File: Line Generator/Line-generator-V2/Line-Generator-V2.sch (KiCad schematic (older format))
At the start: 19 parts, among them J1 Conn_01x04

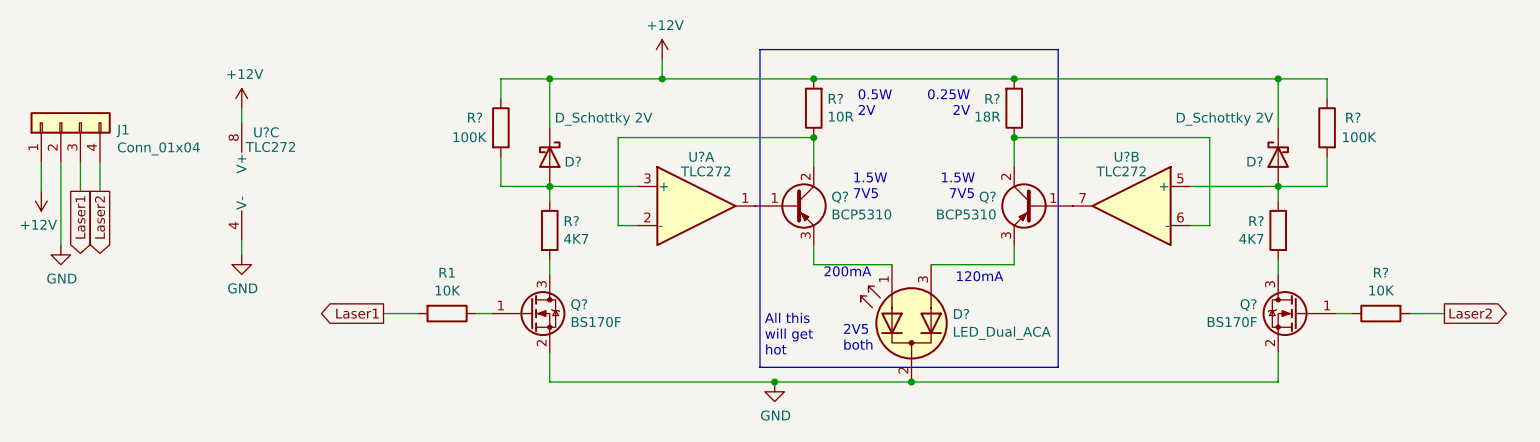
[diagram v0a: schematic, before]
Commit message: Now with 5V power...
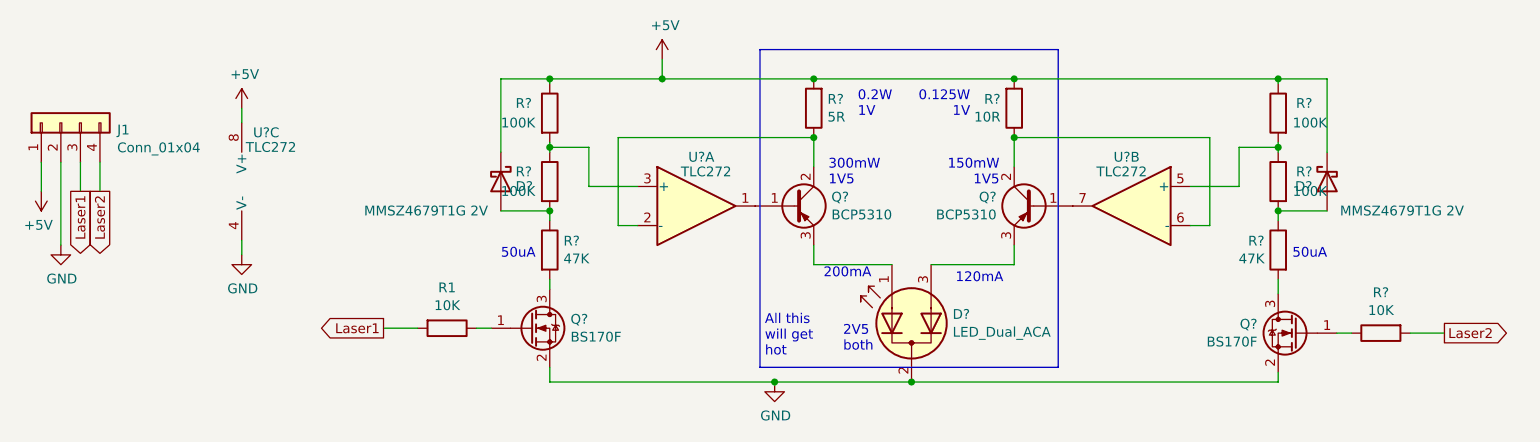
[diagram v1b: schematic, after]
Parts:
- removed D?: D_Schottky 2V, Diode_SMD:D_SOD-323_HandSoldering, symbol Device:D_Schottky
- removed R?: 100K, Resistor_SMD:R_0805_2012Metric_Pad1.15x1.40mm_HandSolder, symbol Device:R
- removed R?: 4K7, Resistor_SMD:R_0805_2012Metric_Pad1.15x1.40mm_HandSolder, symbol Device:R
- added D?: MMSZ4679T1G 2V, Diode_SMD:D_SOD-123, symbol Device:D_Schottky
- added R? (x3): 100K, Resistor_SMD:R_0805_2012Metric_Pad1.15x1.40mm_HandSolder, symbol Device:R
- added R?: 47K, Resistor_SMD:R_0805_2012Metric_Pad1.15x1.40mm_HandSolder, symbol Device:R
- D?: value D_Schottky 2V -> MMSZ4679T1G 2V; footprint Diode_SMD:D_SOD-323_HandSoldering -> Diode_SMD:D_SOD-123
- R?: value 10R -> 5R
- R?: value 4K7 -> 47K
- R?: value 18R -> 10R
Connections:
- net at D?.2 (A), R?.1: now also R?.2; no longer R?.2, U?.3 (+)
- net at U?.5 (+): now also R?.1, R?.2
- net at Q?.3 (D): now also R?.2
- net +12V renamed +5V
- net +5V: now also D?.1 (K), R?.1
- new net: R?.1, R?.2, U?.3 (+)
- new net: D?.2 (A), R?.1, R?.2
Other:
- note added: "0.125W\n1V"
- note added: "0.2W\n1V"
- note added: "150mW\n1V5"
- note added: "300mW\n1V5"
- note added: "50uA"
- note removed: "0.25W\n2V"
- note removed: "0.5W\n2V"
- note removed: "1.5W\n7V5"
- moved on the sheet: D?, Q?, R1, R?

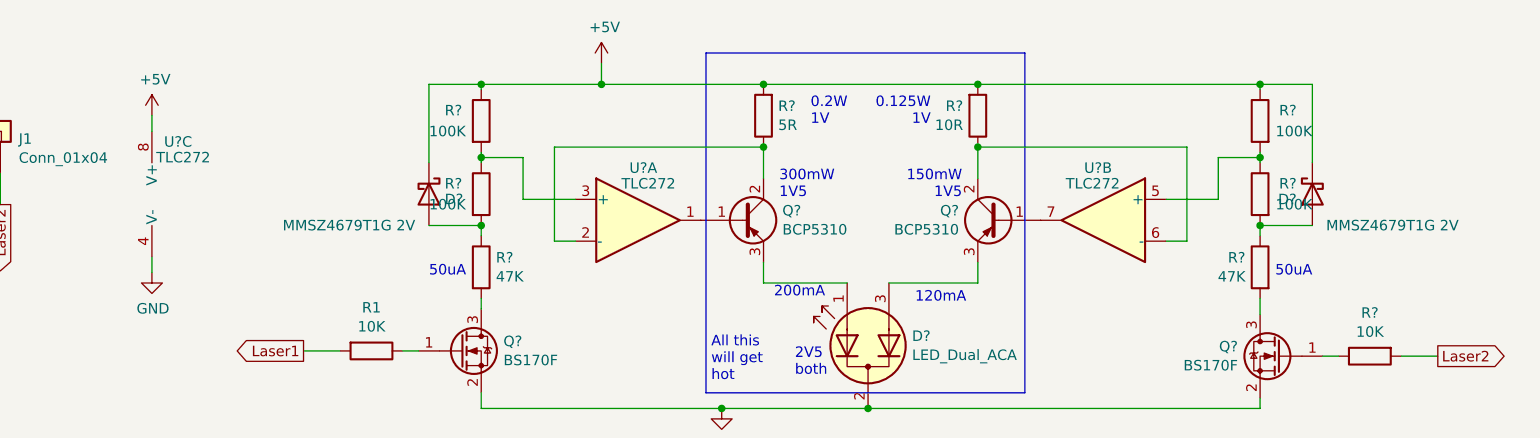
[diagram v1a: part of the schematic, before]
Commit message: Now with adjustable LED current.
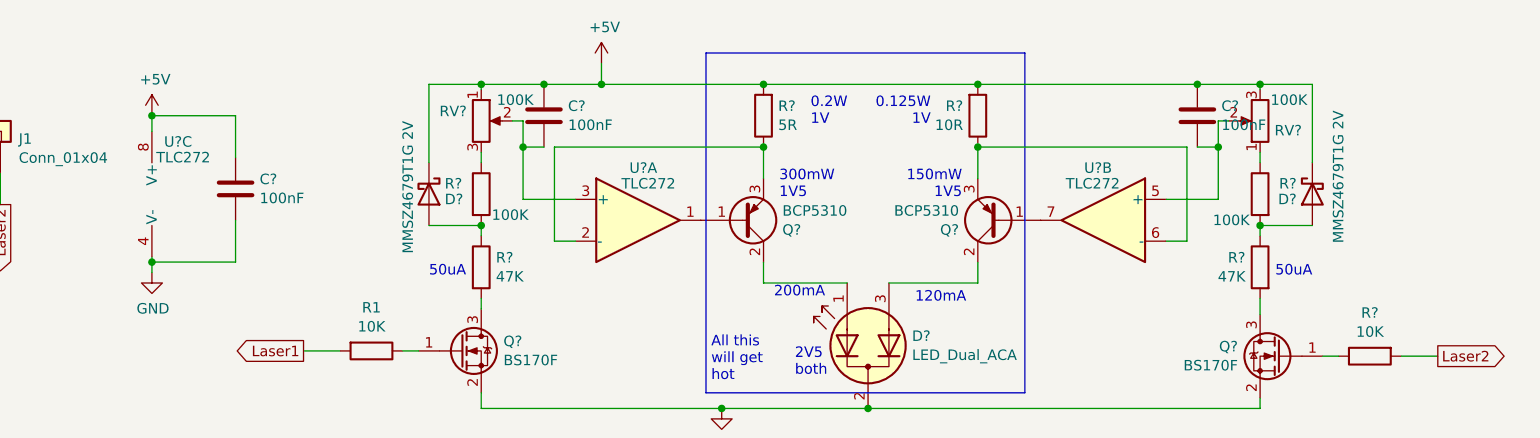
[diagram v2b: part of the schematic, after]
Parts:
- removed R? (x2): 100K, Resistor_SMD:R_0805_2012Metric_Pad1.15x1.40mm_HandSolder, symbol Device:R
- added C? (x3): 100nF, Capacitor_SMD:C_0805_2012Metric, symbol Device:C
- added RV? (x2): 100K, symbol Device:R_POT
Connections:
- net +5V: now also C?.1, C?.1, C?.1, RV?.1, RV?.3
- net GND: now also C?.2
- net at D?.1 (A1): now also Q?.2 (C); no longer Q?.3 (E)
- net at D?.3 (A2): now also Q?.2 (C); no longer Q?.3 (E)
- net at R?.1, U?.2 (-): now also Q?.3 (E); no longer Q?.2 (C)
- net at U?.3 (+): now also C?.2, RV?.2; no longer R?.1
- net at R?.1: now also RV?.1; no longer U?.5 (+)
- net at R?.1, U?.6 (-): now also Q?.3 (E); no longer Q?.2 (C)
- new net: R?.1, RV?.3
- new net: C?.2, RV?.2, U?.5 (+)
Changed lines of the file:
@@
 P 3175 1450
 F 0 "D?" V 3200 1525 50  0000 L CNN
-F 1 "MMSZ4679T1G 2V" V 3325 750 50  0000 L CNN
+F 1 "MMSZ4679T1G 2V" H 2825 1350 50  0000 L CNN
 F 2 "Diode_SMD:D_SOD-123" H 3175 1450 50  0001 C CNN
 F 3 "https://docs.rs-online.com/2159/0900766b812e22b6.pdf" H 3175 1450 50  0001 C CNN
 	1    3175 1450
 	0    1    1    0
-$EndComp
-$Comp
-L Transistor_BJT:BCP51 Q?
-U 1 1 60019DE0
-P 4675 1575
-F 0 "Q?" H 4865 1621 50  0000 L CNN
-F 1 "BCP5310" H 4865 1530 50  0000 L CNN
-F 2 "Package_TO_SOT_SMD:SOT-223-3_TabPin2" H 4875 1500 50  0001 L CIN
-F 3 "" H 4675 1575 50  0001 L CNN
-	1    4675 1575
-	1    0    0    -1
 $EndComp
 $Comp
@@
 Connection ~ 4000 925
 Wire Wire Line
-	4000 925  3425 925
+	4000 925  3725 925
 $Comp
 L Amplifier_Operational:TLC272 U?
@@
 $EndComp
 Wire Wire Line
-	1850 1750 1850 1825
+	1850 1750 1850 1775
 $Comp
 L Transistor_FET:BS170F Q?
@@
 $EndComp
 Connection ~ 4575 2475
-$Comp
-L Device:R R?
-U 1 1 6006FB1E
-P 3425 1100
-F 0 "R?" H 3250 1150 50  0000 L CNN
-F 1 "100K" H 3175 1050 50  0000 L CNN
-F 2 "Resistor_SMD:R_0805_2012Metric_Pad1.15x1.40mm_HandSolder" V 3355 1100 50  0001 C CNN
-F 3 "~" H 3425 1100 50  0001 C CNN
-	1    3425 1100
-	1    0    0    -1
-$EndComp
 $Comp
 L Device:R R?
@@
 F 3 "" H 5900 1575 50  0001 L CNN
 	1    5900 1575
-	-1   0    0    -1
+	-1   0    0    1
 $EndComp
 Text Notes 5725 1475 2    50   ~ 0
@@
 P 3425 1450
 F 0 "R?" H 3250 1500 50  0000 L CNN
-F 1 "100K" H 3175 1400 50  0000 L CNN
+F 1 "100K" H 3475 1350 50  0000 L CNN
 F 2 "Resistor_SMD:R_0805_2012Metric_Pad1.15x1.40mm_HandSolder" V 3355 1450 50  0001 C CNN
 F 3 "~" H 3425 1450 50  0001 C CNN
@@
 	3425 925  3425 950
 Wire Wire Line
-	3425 1250 3425 1275
-Wire Wire Line
 	3425 1600 3425 1650
 Wire Wire Line
@@
 Connection ~ 3425 925
 Wire Wire Line
-	3425 1275 3625 1275
-Wire Wire Line
-	3625 1275 3625 1475
-Wire Wire Line
 	3625 1475 3875 1475
-Connection ~ 3425 1275
-Wire Wire Line
-	3425 1275 3425 1300
 $Comp
 L Device:D_Schottky D?
@@
 P 7400 1450
 F 0 "D?" V 7425 1525 50  0000 L CNN
-F 1 "MMSZ4679T1G 2V" V 7550 750 50  0000 L CNN
+F 1 "MMSZ4679T1G 2V" H 7000 1325 50  0000 L CNN
 F 2 "Diode_SMD:D_SOD-123" H 7400 1450 50  0001 C CNN
 F 3 "https://docs.rs-online.com/2159/0900766b812e22b6.pdf" H 7400 1450 50  0001 C CNN
 	1    7400 1450
 	0    -1   1    0
-$EndComp
-$Comp
-L Device:R R?
-U 1 1 60097201
-P 7150 1100
-F 0 "R?" H 6975 1150 50  0000 L CNN
-F 1 "100K" H 6900 1050 50  0000 L CNN
-F 2 "Resistor_SMD:R_0805_2012Metric_Pad1.15x1.40mm_HandSolder" V 7080 1100 50  0001 C CNN
-F 3 "~" H 7150 1100 50  0001 C CNN
-	1    7150 1100
-	-1   0    0    -1
 $EndComp
 $Comp
@@
 P 7150 1450
 F 0 "R?" H 6975 1500 50  0000 L CNN
-F 1 "100K" H 6900 1400 50  0000 L CNN
+F 1 "100K" H 7200 1325 50  0000 L CNN
 F 2 "Resistor_SMD:R_0805_2012Metric_Pad1.15x1.40mm_HandSolder" V 7080 1450 50  0001 C CNN
 F 3 "~" H 7150 1450 50  0001 C CNN
@@
 	7150 925  7150 950
 Wire Wire Line
-	7150 1250 7150 1275
-Wire Wire Line
 	7150 1600 7150 1650
 Wire Wire Line
@@
 Connection ~ 7150 925
 Wire Wire Line
-	7150 1275 6950 1275
-Wire Wire Line
-	6950 1275 6950 1475
-Wire Wire Line
 	6950 1475 6700 1475
-Connection ~ 7150 1275
-Wire Wire Line
-	7150 1275 7150 1300
-Wire Wire Line
-	5800 925  7150 925
+Wire Wire Line
+	5800 925  6850 925
 Connection ~ 5800 925
 Wire Wire Line
@@
 Wire Wire Line
 	7150 2425 7150 2475
+Wire Wire Line
+	3425 1250 3425 1300
+$Comp
+L Device:R_POT RV?
+U 1 1 6000B3BD
+P 3425 1100
+F 0 "RV?" H 3356 1146 50  0000 R CNN
+F 1 "100K" H 3675 1200 50  0000 R CNN
+F 2 "" H 3425 1100 50  0001 C CNN
+F 3 "~" H 3425 1100 50  0001 C CNN
+	1    3425 1100
+	1    0    0    -1
+$EndComp
+Wire Wire Line
+	3575 1100 3625 1100
+$Comp
+L Device:R_POT RV?
+U 1 1 60010BB5
+P 7150 1100
+F 0 "RV?" H 7081 1146 50  0000 R CNN
+F 1 "100K" H 7100 1000 50  0000 R CNN
+F 2 "" H 7150 1100 50  0001 C CNN
+F 3 "~" H 7150 1100 50  0001 C CNN
+	1    7150 1100
+	-1   0    0    1
+$EndComp
+Wire Wire Line
+	7150 1250 7150 1300
+Wire Wire Line
+	7000 1100 6950 1100
+Wire Wire Line
+	6950 1100 6950 1225
+$Comp
+L Device:C C?
+U 1 1 60017144
+P 2250 1425
+F 0 "C?" H 2365 1471 50  0000 L CNN
+F 1 "100nF" H 2365 1380 50  0000 L CNN
+F 2 "Capacitor_SMD:C_0805_2012Metric" H 2288 1275 50  0001 C CNN
+F 3 "~" H 2250 1425 50  0001 C CNN
+	1    2250 1425
+	1    0    0    -1
+$EndComp
+$Comp
+L Device:C C?
+U 1 1 60017FDE
+P 3725 1075
+F 0 "C?" H 3840 1121 50  0000 L CNN
+F 1 "100nF" H 3840 1030 50  0000 L CNN
+F 2 "Capacitor_SMD:C_0805_2012Metric" H 3763 925 50  0001 C CNN
+F 3 "~" H 3725 1075 50  0001 C CNN
+	1    3725 1075
+	1    0    0    -1
+$EndComp
+Connection ~ 3725 925
+Wire Wire Line
+	3725 925  3425 925
+$Comp
+L Device:C C?
+U 1 1 60018C52
+P 6850 1075
+F 0 "C?" H 6965 1121 50  0000 L CNN
+F 1 "100nF" H 6965 1030 50  0000 L CNN
+F 2 "Capacitor_SMD:C_0805_2012Metric" H 6888 925 50  0001 C CNN
+F 3 "~" H 6850 1075 50  0001 C CNN
+	1    6850 1075
+	1    0    0    -1
+$EndComp
+Connection ~ 6850 925
+Wire Wire Line
+	6850 925  7150 925
+Wire Wire Line
+	6850 1225 6950 1225
+Connection ~ 6950 1225
+Wire Wire Line
+	6950 1225 6950 1475
+Wire Wire Line
+	3725 1225 3625 1225
+Wire Wire Line
+	3625 1100 3625 1225
+Connection ~ 3625 1225
+Wire Wire Line
+	3625 1225 3625 1475
+Wire Wire Line
+	1850 1075 2250 1075
+Wire Wire Line
+	2250 1075 2250 1275
+Connection ~ 1850 1075
+Wire Wire Line
+	1850 1775 2250 1775
+Wire Wire Line
+	2250 1775 2250 1575
+Connection ~ 1850 1775
+Wire Wire Line
+	1850 1775 1850 1825
+$Comp
+L Transistor_BJT:BCP51 Q?
+U 1 1 60019DE0
+P 4675 1575
+F 0 "Q?" H 4865 1621 50  0000 L CNN
+F 1 "BCP5310" H 4865 1530 50  0000 L CNN
+F 2 "Package_TO_SOT_SMD:SOT-223-3_TabPin2" H 4875 1500 50  0001 L CIN
+F 3 "" H 4675 1575 50  0001 L CNN
+	1    4675 1575
+	1    0    0    1
+$EndComp
 $EndSCHEMATC

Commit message: Latest laser circuit. Maybe final?!?
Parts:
- Q2, Q3: renamed from Q?; value BCP5310 -> SS8550
- R2: renamed from R?; value 100K -> 82K
- R4: renamed from R?; value 5R -> 4R7
- gave numbers to parts that had none: 16
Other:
- note added: "2V5"
- note added: "300mW"
- note added: "500mW"
- note added: "All this\nwill get\nslightly\nhot"
- note removed: "2V5\nboth"
- note removed: "All this\nwill get\nhot"
- moved on the sheet: C1, C2, C3, D1, D2, D3, J1, Q1, Q2, Q3, Q4, R1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

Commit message: Minor changes
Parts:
- added H1, H4: MountingHole_Pad, MountingHole:MountingHole_3.2mm_M3_DIN965_Pad, symbol Mechanical:MountingHole_Pad
- J1: footprint Connector_JST:JST_PH_B4B-PH-SM4-TB_1x04-1MP_P2.00mm_Vertical -> Connector_JST:JST_XH_B4B-XH-A_1x04_P2.50mm_Vertical
- Q2, Q3: value SS8550 -> BCP5310
- R2: value 82K -> 100K
- R4: value 4R7 -> 5R
- RV1, RV2: footprint (none) -> Potentiometer_THT:Potentiometer_Bourns_3386C_Horizontal
- U1: footprint (none) -> Package_SO:SOIC-8_3.9x4.9mm_P1.27mm
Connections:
- net GND: now also H1.1, H4.1
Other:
- note added: "2V5\nboth"
- note added: "All this\nwill get\nhot"
- note removed: "2V5"
- note removed: "300mW"
- note removed: "500mW"
- note removed: "All this\nwill get\nslightly\nhot"
- moved on the sheet: C1, C2, C3, D1, D2, D3, J1, Q1, Q2, Q3, Q4, R1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
